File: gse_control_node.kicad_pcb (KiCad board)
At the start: 4 copper layers, 65 x 65 mm, 119 parts, among them J1 Screw_Terminal_01x02, J10 Conn_01x02, J2 Conn_01x04, J3 Conn_01x04, J4 Conn_02x01, J5 USB_C_Receptacle_USB2.0_16P, J6 Conn_01x04, J7 Conn_01x02, J8 Conn_01x02, J9 Conn_01x02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

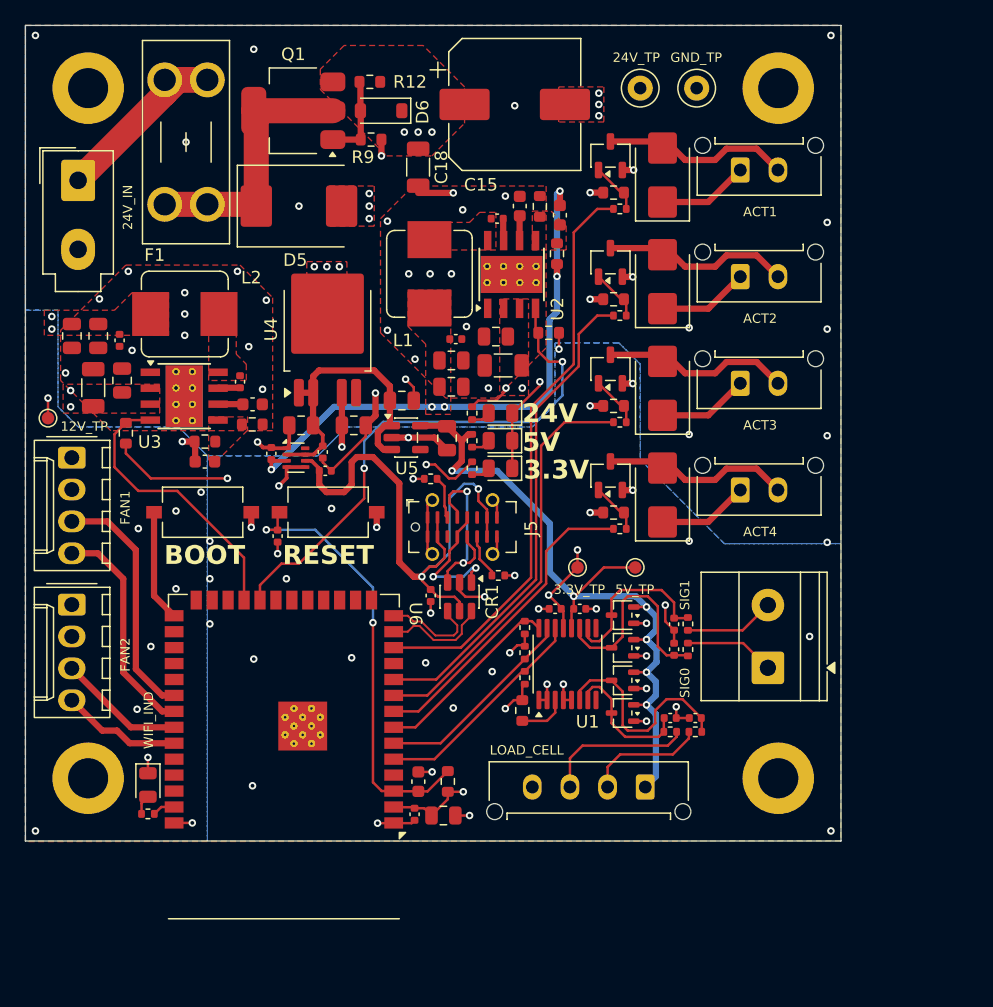
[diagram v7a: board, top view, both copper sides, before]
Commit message: update resistors to jlcpcb basic components
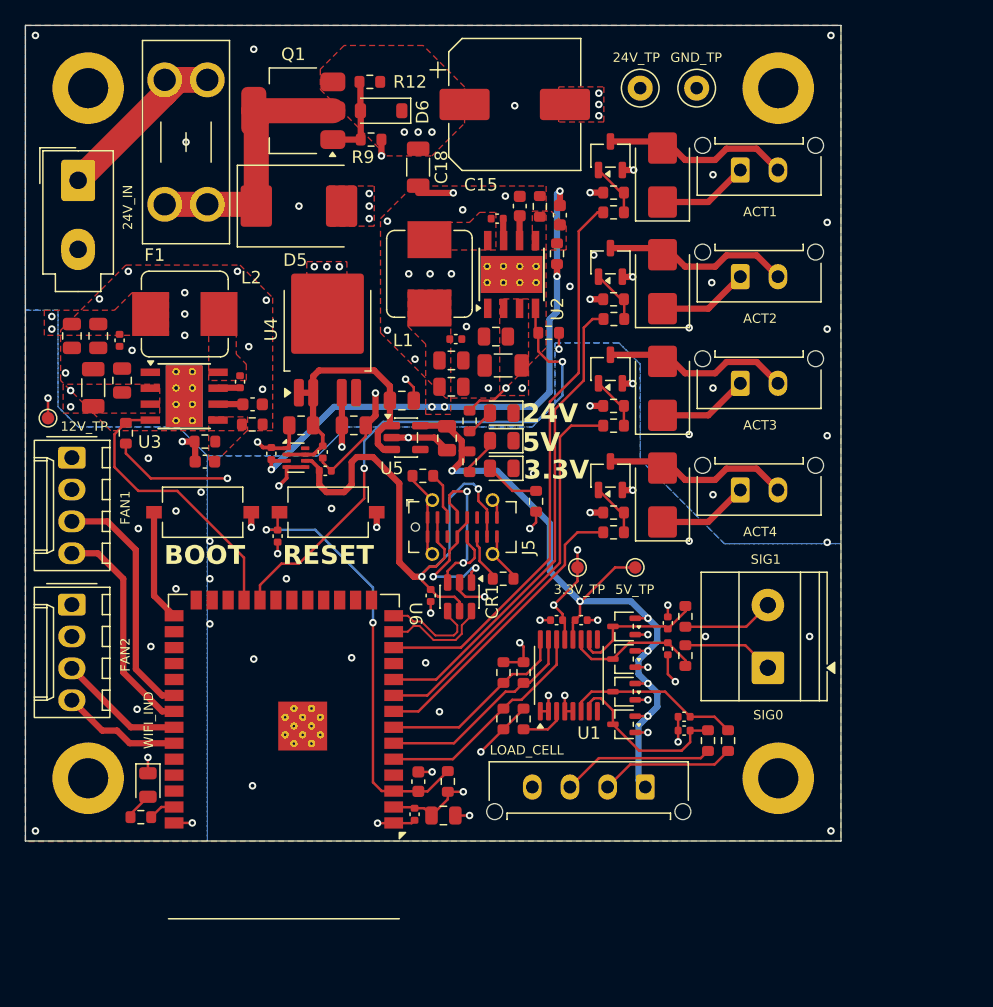
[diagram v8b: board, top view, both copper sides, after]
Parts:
- R1, R17, R18, R19, R2, R21, R22, R23, R24, R26, R28, R3, R30, R4, R5, R6, R7: footprint Resistor_SMD:R_0402_1005Metric -> Resistor_SMD:R_0603_1608Metric
- moved R18 5.74 mm to (104.4, 54.5), turned to -90 degrees
- moved R2 3.97 mm to (101.8, 68.2), turned to 90 degrees
- moved R1 3.70 mm to (101.8, 71.9)
- moved R5 3.09 mm to (118.1, 73.6), turned to 90 degrees
- moved R4 2.70 mm to (119.7, 73.6), turned to 90 degrees
- moved R19 1.69 mm to (99.1, 51.4)
- moved R3 1.59 mm to (103.4, 68.2)
- moved C5 1.49 mm to (116.2, 72.8), turned to 180 degrees
- moved U1 0.91 mm to (107.0, 68.4)
- moved D1 0.91 mm to (111.4, 69.7)
- moved C1 0.91 mm to (106.0, 64.0)
- moved C2 0.91 mm to (108.0, 64.0)
- moved D4 0.91 mm to (111.4, 64.5)
- moved D2 0.91 mm to (111.4, 67.1)
- moved D3 0.91 mm to (111.4, 72.3)
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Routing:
- net /ADC 1/AIN0: track 16.8 -> 11.0 mm
- net GND: track 82.2 -> 78.0 mm, vias 101 -> 107
- net /ADC 1/AIN2: track 10.9 -> 14.3 mm
- net /ADC 1/AIN3: track 17.4 -> 14.1 mm
- net Net-(D8-A): track 1.53 -> 4.42 mm
- net /ADC 1/AIN1: track 13.5 -> 11.1 mm
- net Net-(D9-A): track 1.54 -> 3.17 mm
- net ACTUATOR_4_CTL: track 25.1 -> 23.5 mm
- net ACTUATOR_3_CTL: track 32.9 -> 31.5 mm
- net LOAD_CELL+: track 9.54 -> 10.8 mm
- net ACTUATOR_1_CTL: track 46.1 -> 45.0 mm
- net ACTUATOR_2_CTL: track 39.0 -> 38.2 mm
- net +5V: track 59.3 -> 58.5 mm
- net Net-(D7-A): track 1.54 -> 2.23 mm
- net Net-(D10-A): track 1.57 -> 2.20 mm
